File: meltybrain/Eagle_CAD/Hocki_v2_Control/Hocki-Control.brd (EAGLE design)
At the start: 90 x 46 mm, 150 parts, among them CN1 JST_2PIN, J1 SM03B-SRSS-TB(LF)(SN), J2 SM04B-SRSS-TB(LF)(SN), J4 SM04B-SRSS-TB(LF)(SN), J5 SM03B-SRSS-TB(LF)(SN), J6 SM03B-SRSS-TB(LF)(SN), J7 SM02B-SRSS-TB(LF)(SN), J8 SM02B-SRSS-TB(LF)(SN), U1 AP63200, U10 LMH6612MAX/NOPB, U11 TLV3502AIDCNR, U12 LMH6612MAX/NOPB, U13 TMP235A4DCKR, U14 ADXL375, U15 NL27WZ32USG, U16 ADXL375, U17 ADXL375, U18 NL27WZ32USG, U19 ADXL375, U2 TEENSY_4.1, U20 AD8426ACPZ-WP, U21 LMH6612MAX/NOPB, U22 HMC1052L-TR, U23 LMH6612MAX/NOPB, U24 IRF7509, U25 LIS3MDLTR, U3 AP2210K-5.0TRG1, U4 AP2210K-3.3TRG1, U5 TXS0104ED, U6 LDL212PU50R, U7 LMH6612MAX/NOPB, U8 LMH6612MAX/NOPB, U9 TMUX1219DCKR

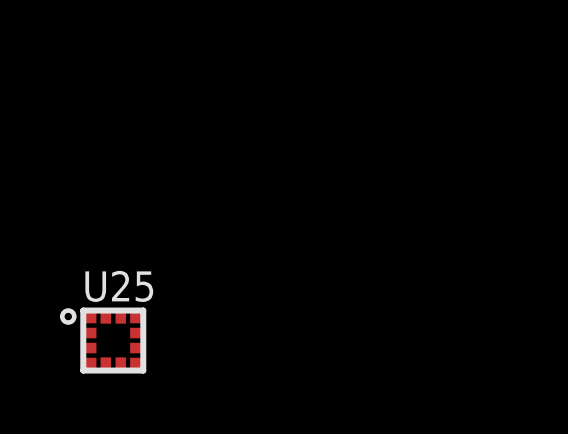
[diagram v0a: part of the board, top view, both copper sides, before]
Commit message: route schematic for new magnetometer, remove IR capabilities and old magnetometer
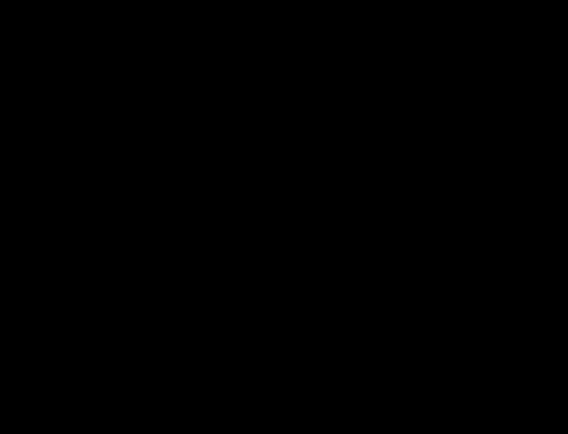
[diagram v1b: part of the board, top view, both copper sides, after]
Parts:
- removed U25: LIS3MDLTR, Hocki_Library:LGA-12_2X2X1_STM
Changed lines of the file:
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@@
 <attribute name="VALUE" x="16" y="9" size="1" layer="27" font="vector" ratio="10" rot="R270" align="top-left"/>
-</element>
-<element name="U25" library="Hocki_Library" package="LGA-12_2X2X1_STM" value="LIS3MDLTR" x="-55" y="-40" smashed="yes">
-<attribute name="DKPN" value="497-13892-1-ND" x="-55" y="-40" size="1.778" layer="27" display="off"/>
-<attribute name="NAME" x="-56.0366" y="-38.695" size="1" layer="25" font="vector" ratio="10" rot="SR0"/>
-<attribute name="VALUE" x="-56.0272" y="-41.335" size="1" layer="27" font="vector" ratio="10" rot="SR0" align="top-left"/>
 </element>
 </elements>
